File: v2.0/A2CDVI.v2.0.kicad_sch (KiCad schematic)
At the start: 33 parts, among them CON3 Apple2_edge_connector, J1 DA15_Plug, J2 Aux, U1 RPI-Pico, U2 74LVC245, U3 74LVC245, U4 74LVC245, U5 74LVC245

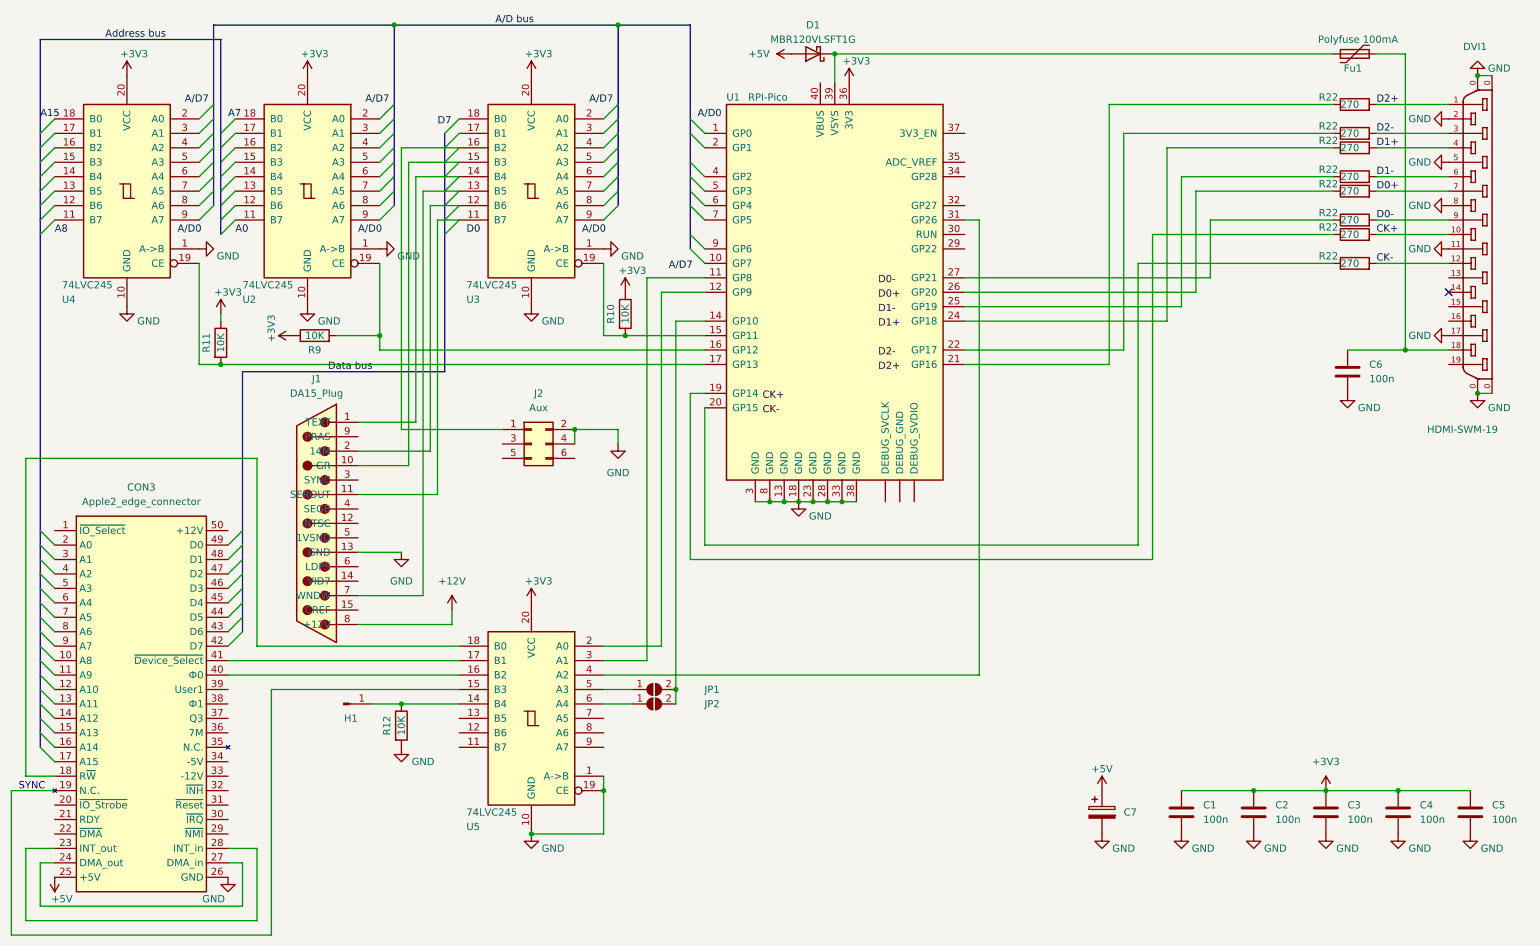
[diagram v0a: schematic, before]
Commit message: Update A2CDVI.v2.0.kicad_sch
Added components, removed Slot and extra 245 chips
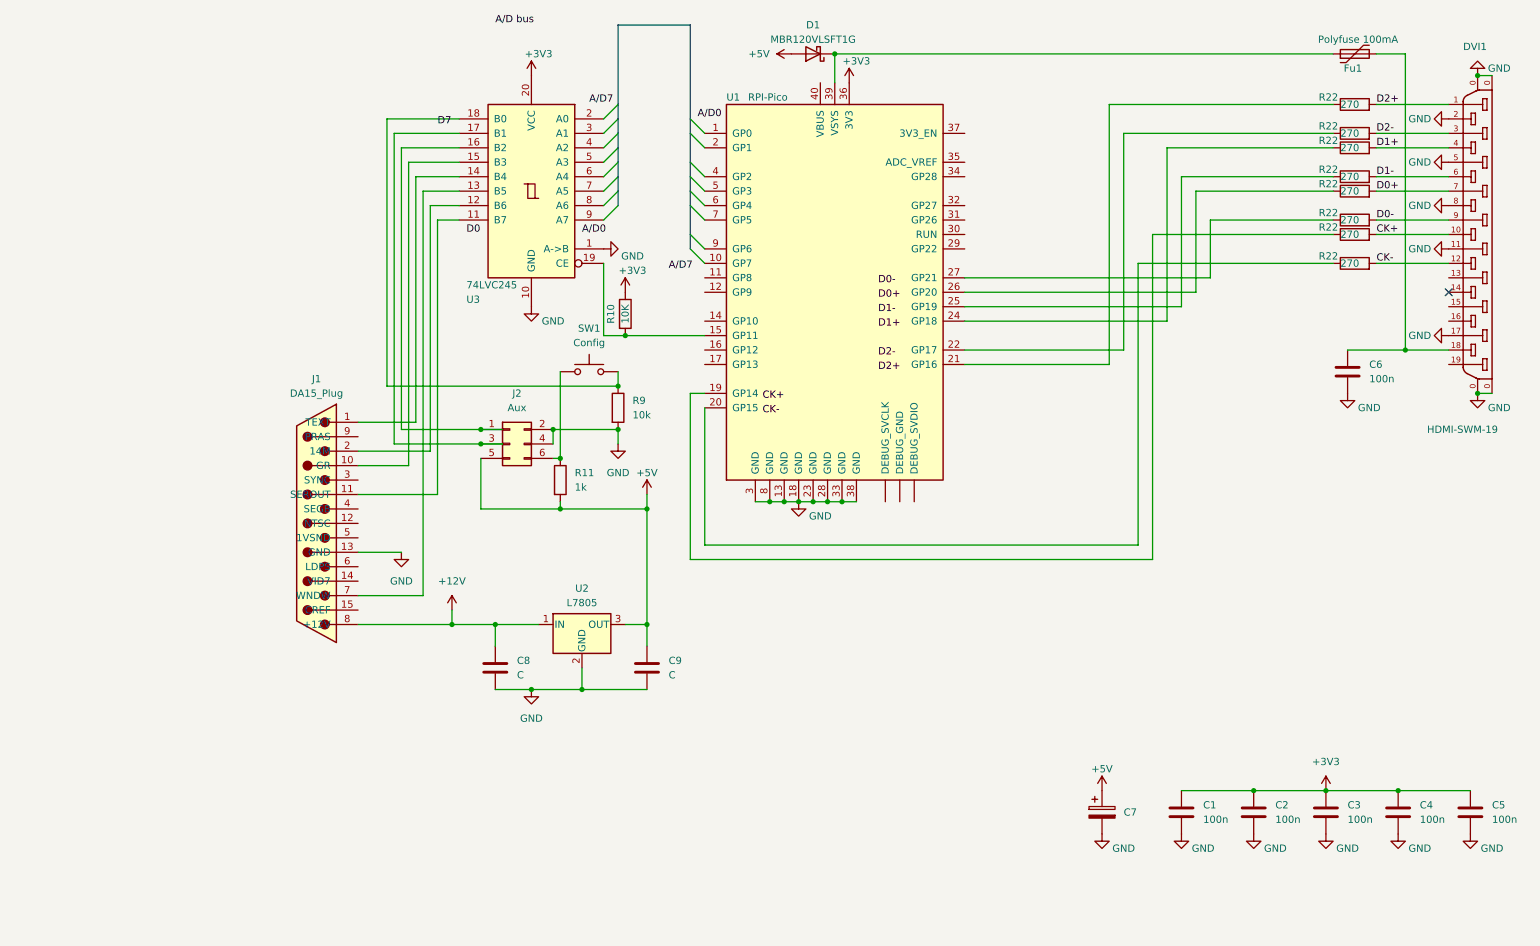
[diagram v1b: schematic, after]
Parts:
- removed CON3: Apple2_edge_connector, AppleII:Connector Apple II, symbol Ralle_Library:Apple2_edge_connector
- removed H1: Conn_01x01_Pin, symbol Connector:Conn_01x01_Pin
- removed JP1, JP2: SolderJumper_2_Open, symbol Jumper:SolderJumper_2_Open
- removed R12: 10K, Resistor_SMD:R_0402_1005Metric_Pad0.72x0.64mm_HandSolder, symbol Device:R
- removed U2, U4, U5: 74LVC245, symbol 74xx:74LS245
- added C8, C9: C, symbol Device:C
- added SW1: Config, symbol Switch:SW_Push
- added U2: L7805, symbol Regulator_Linear:L7805
- R11: value 10K -> 1k; footprint Resistor_SMD:R_0402_1005Metric_Pad0.72x0.64mm_HandSolder -> (none)
- R9: value 10K -> 10k; footprint Resistor_SMD:R_0402_1005Metric_Pad0.72x0.64mm_HandSolder -> (none)
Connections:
- net +12V: now also C8.1, U2.1 (IN)
- net +3V3: no longer R11.1, R9.1
- net +5V: now also J2.5 (Pin_5), R11.2, C9.1, U2.3 (OUT)
- net GND: now also R9.2, C8.2, C9.2, U2.2 (GND)
- net at J2.3 (Pin_3): now also U3.17 (B1)
- net at J2.6 (Pin_6): now also R11.1, SW1.1
- net at U1.17 (GP13): no longer R11.2
- net at U1.16 (GP12): no longer R9.2
- net at U3.18 (B0): now also R9.1, SW1.2
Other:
- note removed: "SYNC"
- moved on the sheet: J2

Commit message: Initial Layout mess
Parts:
- C1, C2, C3, C4, C5, C6, C8, C9: footprint (none) -> Capacitor_SMD:C_0402_1005Metric_Pad0.74x0.62mm_HandSolder
- C7: footprint (none) -> Capacitor_SMD:C_1210_3225Metric_Pad1.33x2.70mm_HandSolder
- DVI1: footprint (none) -> Connector_Video:HDMI_A_Molex_208658-1001_Horizontal
- Fu1: footprint (none) -> Fuse:Fuse_0805_2012Metric_Pad1.15x1.40mm_HandSolder
- J1: footprint (none) -> Connector_Dsub:DSUB-15_Male_Vertical_P2.77x2.84mm_MountingHoles
- J2: footprint (none) -> Connector_PinHeader_1.00mm:PinHeader_2x03_P1.00mm_Vertical
- R11, R22, R9: footprint (none) -> Resistor_SMD:R_0402_1005Metric_Pad0.72x0.64mm_HandSolder
- SW1: footprint (none) -> Button_Switch_SMD:SW_SPST_PTS645
- U1: footprint (none) -> MCU_RaspberryPi_and_Boards:RPi_Pico_SMD_TH
- U2: footprint (none) -> Package_TO_SOT_SMD:TO-252-2
- U3: footprint (none) -> Package_SO:TSSOP-20_4.4x6.5mm_P0.65mm
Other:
- moved on the sheet: C1, C2, C3, C4, C5, C7

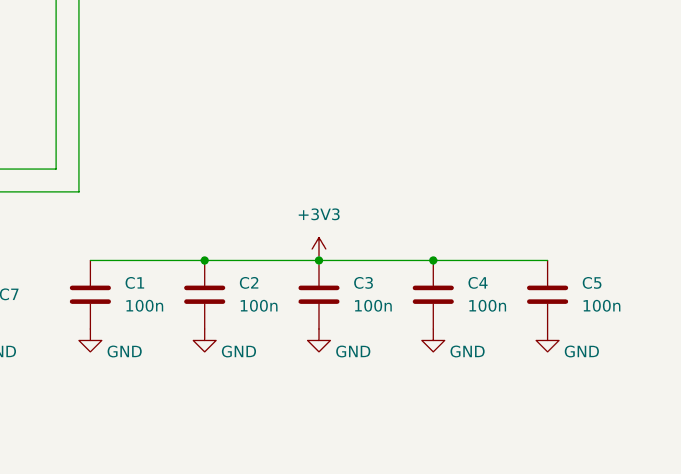
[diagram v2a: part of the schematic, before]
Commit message: Basic Board Layout
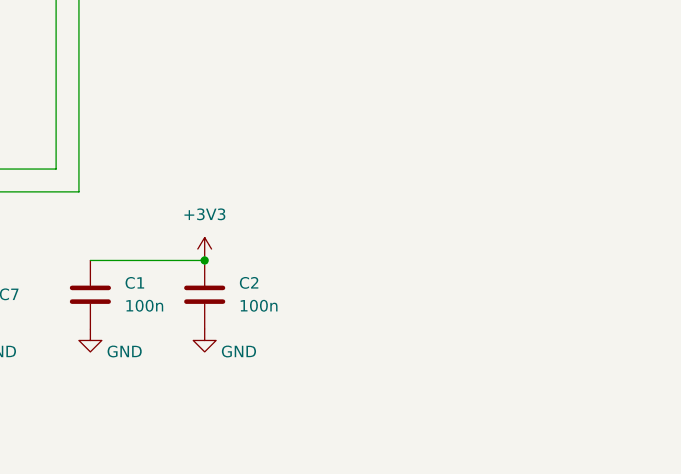
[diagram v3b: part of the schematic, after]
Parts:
- removed C3, C4, C5: 100n, Capacitor_SMD:C_0402_1005Metric_Pad0.74x0.62mm_HandSolder, symbol Device:C
- D1: footprint Diode_THT:D_DO-35_SOD27_P7.62mm_Horizontal -> Diode_SMD:D_SMA_Handsoldering
- J2: footprint Connector_PinHeader_1.00mm:PinHeader_2x03_P1.00mm_Vertical -> Connector_PinHeader_2.54mm:PinHeader_2x03_P2.54mm_Vertical
- R10, R11, R22, R9: footprint Resistor_SMD:R_0402_1005Metric_Pad0.72x0.64mm_HandSolder -> Resistor_SMD:R_0402_1005Metric
- U1: footprint MCU_RaspberryPi_and_Boards:RPi_Pico_SMD_TH -> MCU_RaspberryPi_and_Boards:RPi_Pico_SMD_TH_NO_DEBUG

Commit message: Tracks drawn
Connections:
- net +12V: now also Fu1.2; no longer J1.8 (+12V)
- net CK+: now also R22.1, U1.19 (GP14)
- net CK-: now also R22.1, U1.20 (GP15)
- net D0+: now also R22.1, U1.26 (GP20)
- net D0-: now also R22.1, U1.27 (GP21)
- net D1+: now also R22.1, U1.24 (GP18)
- net D1-: now also R22.1, U1.25 (GP19)
- net D2+: now also R22.1, U1.21 (GP16)
- net D2-: now also R22.1, U1.22 (GP17)
- net at D1.1 (K), U1.39 (VSYS): no longer Fu1.1
- net at C6.1, DVI1.18: no longer Fu1.2
- new net: Fu1.1, J1.8 (+12V)
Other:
- moved on the sheet: Fu1
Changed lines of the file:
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@@
 	)
 	(junction
-		(at 151.13 100.33)
+		(at 275.59 81.28)
 		(diameter 0)
 		(color 0 0 0 0)
 	)
 	(junction
-		(at 156.21 100.33)
+		(at 151.13 100.33)
 		(diameter 0)
 		(color 0 0 0 0)
 	)
 	(junction
-		(at 260.35 73.66)
+		(at 156.21 100.33)
 		(diameter 0)
 		(color 0 0 0 0)
@@
 		(color 0 0 0 0)
 	)
-	(junction
-		(at 160.02 21.59)
-		(diameter 0)
-		(color 0 0 0 0)
-	)
 	(no_connect
 		(at 267.97 63.5)
@@
 	(wire
 		(pts
+			(xy 88.9 121.92) (xy 92.71 121.92)
+		)
+		(stroke
+			(width 0)
+			(type default)
+		)
+	)
+	(wire
+		(pts
 			(xy 267.97 45.72) (xy 255.27 45.72)
 		)
@@
 		)
 	)
+	(wire
+		(pts
+			(xy 280.67 82.55) (xy 280.67 81.28)
+		)
+		(stroke
+			(width 0)
+			(type default)
+		)
+	)
 	(bus
 		(pts
@@
 	(wire
 		(pts
+			(xy 237.49 20.32) (xy 237.49 21.59)
+		)
+		(stroke
+			(width 0)
+			(type default)
+		)
+	)
+	(wire
+		(pts
 			(xy 100.33 133.35) (xy 106.68 133.35)
 		)
@@
 	(wire
 		(pts
-			(xy 260.35 73.66) (xy 267.97 73.66)
-		)
-		(stroke
-			(width 0)
-			(type default)
-		)
-	)
-	(wire
-		(pts
 			(xy 215.9 53.34) (xy 215.9 110.49)
 		)
@@
 	(wire
 		(pts
-			(xy 260.35 21.59) (xy 260.35 73.66)
-		)
-		(stroke
-			(width 0)
-			(type default)
-		)
-	)
-	(wire
-		(pts
 			(xy 213.36 58.42) (xy 247.65 58.42)
 		)
@@
 	(wire
 		(pts
-			(xy 123.19 71.12) (xy 137.16 71.12)
+			(xy 280.67 81.28) (xy 275.59 81.28)
 		)
 		(stroke
@@
 	(wire
 		(pts
-			(xy 255.27 21.59) (xy 260.35 21.59)
+			(xy 123.19 71.12) (xy 137.16 71.12)
 		)
 		(stroke
@@
 	(wire
 		(pts
-			(xy 160.02 21.59) (xy 247.65 21.59)
-		)
-		(stroke
-			(width 0)
-			(type default)
-		)
-	)
-	(wire
-		(pts
 			(xy 82.55 90.17) (xy 82.55 35.56)
 		)
@@
 	(wire
 		(pts
-			(xy 250.19 73.66) (xy 260.35 73.66)
+			(xy 250.19 73.66) (xy 267.97 73.66)
 		)
 		(stroke
@@
 	(wire
 		(pts
-			(xy 76.2 121.92) (xy 92.71 121.92)
+			(xy 273.05 82.55) (xy 273.05 81.28)
+		)
+		(stroke
+			(width 0)
+			(type default)
+		)
+	)
+	(wire
+		(pts
+			(xy 76.2 121.92) (xy 81.28 121.92)
 		)
 		(stroke
@@
 	)
 	(label "CK-"
-		(at 147.32 85.09 0)
+		(at 137.16 86.36 0)
+		(fields_autoplaced yes)
+		(effects
+			(font
+				(size 1.27 1.27)
+			)
+			(justify left bottom)
+		)
+	)
+	(label "D2+"
+		(at 182.88 76.2 0)
 		(fields_autoplaced yes)
 		(effects
@@
 	)
 	(label "D1-"
-		(at 167.64 67.31 0)
+		(at 182.88 66.04 0)
 		(fields_autoplaced yes)
 		(effects
@@
 	)
 	(label "D0-"
-		(at 167.64 62.23 0)
+		(at 182.88 60.96 0)
 		(fields_autoplaced yes)
 		(effects
@@
 	)
 	(label "D0+"
-		(at 167.64 64.77 0)
+		(at 182.88 63.5 0)
 		(fields_autoplaced yes)
 		(effects
@@
 	)
 	(label "CK+"
-		(at 147.32 82.55 0)
+		(at 134.62 81.28 0)
+		(fields_autoplaced yes)
+		(effects
+			(font
+				(size 1.27 1.27)
+			)
+			(justify left bottom)
+		)
+	)
+	(label "D2-"
+		(at 182.88 73.66 0)
 		(fields_autoplaced yes)
 		(effects
@@
 	)
 	(label "D1+"
-		(at 167.64 69.85 0)
+		(at 182.88 68.58 0)
 		(fields_autoplaced yes)
 		(effects
@@
 	(symbol
 		(lib_id "Neo6502_Rev_B:GND")
+		(at 280.67 82.55 0)
+		(unit 1)
+		(exclude_from_sim no)
+		(in_bom yes)
+		(on_board yes)
+		(dnp no)
+		(property "Reference" "#PWR08"
+			(at 280.67 88.9 0)
+			(effects
+				(font
+					(size 1.27 1.27)
+				)
+				(hide yes)
+			)
+		)
+		(property "Value" "GND"
+			(at 280.67 87.63 90)
+			(effects
+				(font
+					(size 1.27 1.27)
+				)
+			)
+		)
+		(property "Footprint" ""
+			(at 280.67 82.55 0)
+			(effects
+				(font
+					(size 1.524 1.524)
+				)
+			)
+		)
+		(property "Datasheet" ""
+			(at 280.67 82.55 0)
+			(effects
+				(font
+					(size 1.524 1.524)
+				)
+			)
+		)
+		(property "Description" ""
+			(at 280.67 82.55 0)
+			(effects
+				(font
+					(size 1.27 1.27)
+				)
+				(hide yes)
+			)
+		)
+		(pin "1"
+		)
+		(instances
+			(project "A2CDVI.v2.0"
+				(path "/4c6c2bca-2dd1-4d7b-a3c3-50b1d850646e"
+					(reference "#PWR08")
+					(unit 1)
+				)
+			)
+		)
+	)
+	(symbol
+		(lib_id "Neo6502_Rev_B:GND")
 		(at 267.97 40.64 270)
 		(mirror x)
@@
 	(symbol
 		(lib_id "Device:Polyfuse")
-		(at 251.46 21.59 90)
+		(at 85.09 121.92 90)
 		(unit 1)
 		(exclude_from_sim no)
@@
 		(dnp no)
 		(property "Reference" "Fu1"
-			(at 252.73 24.13 90)
+			(at 86.36 124.46 90)
 			(effects
 				(font
@@
 		)
 		(property "Value" "Polyfuse 100mA"
-			(at 259.08 19.05 90)
+			(at 92.71 119.38 90)
 			(effects
 				(font
@@
 		)
 		(property "Footprint" "Fuse:Fuse_0805_2012Metric_Pad1.15x1.40mm_HandSolder"
-			(at 256.54 20.32 0)
+			(at 90.17 120.65 0)
 			(effects
 				(font
@@
 		)
 		(property "Datasheet" "MF-R020"
-			(at 251.46 21.59 0)
+			(at 85.09 121.92 0)
 			(effects
 				(font
@@
 		)
 		(property "Description" ""
-			(at 251.46 21.59 0)
+			(at 85.09 121.92 0)
 			(effects
 				(font
@@
 	(symbol
 		(lib_id "Neo6502_Rev_B:GND")
-		(at 273.05 81.28 0)
+		(at 273.05 82.55 0)
 		(mirror y)
 		(unit 1)
@@
 		(dnp no)
 		(property "Reference" "#PWR?"
-			(at 273.05 87.63 0)
+			(at 273.05 88.9 0)
 			(effects
 				(font
@@
 		)
 		(property "Value" "GND"
-			(at 276.86 83.82 0)
+			(at 276.86 85.09 0)
 			(effects
 				(font
@@
 		)
 		(property "Footprint" ""
-			(at 273.05 81.28 0)
+			(at 273.05 82.55 0)
 			(effects
 				(font
@@
 		)
 		(property "Datasheet" ""
-			(at 273.05 81.28 0)
+			(at 273.05 82.55 0)
 			(effects
 				(font
@@
 		)
 		(property "Description" ""
-			(at 273.05 81.28 0)
+			(at 273.05 82.55 0)
 			(effects
 				(font

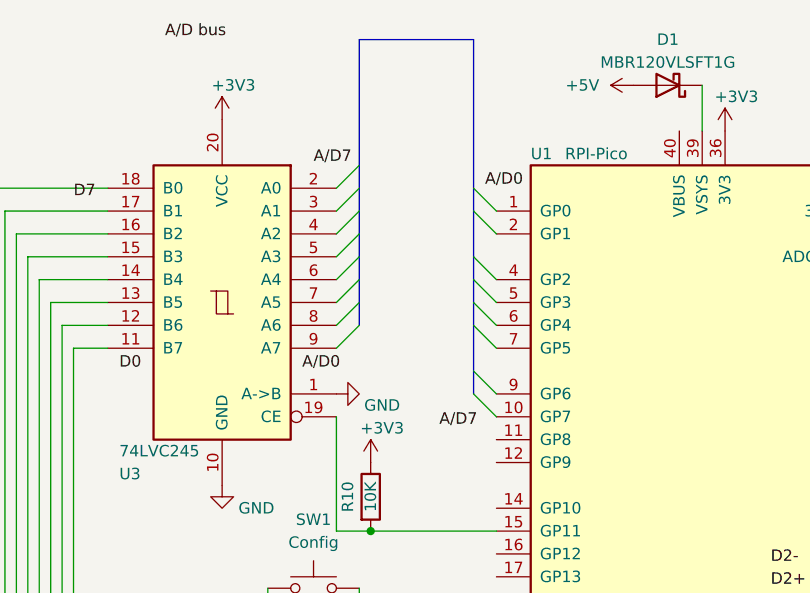
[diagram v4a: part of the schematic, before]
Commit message: Fixed missing connections in schematic
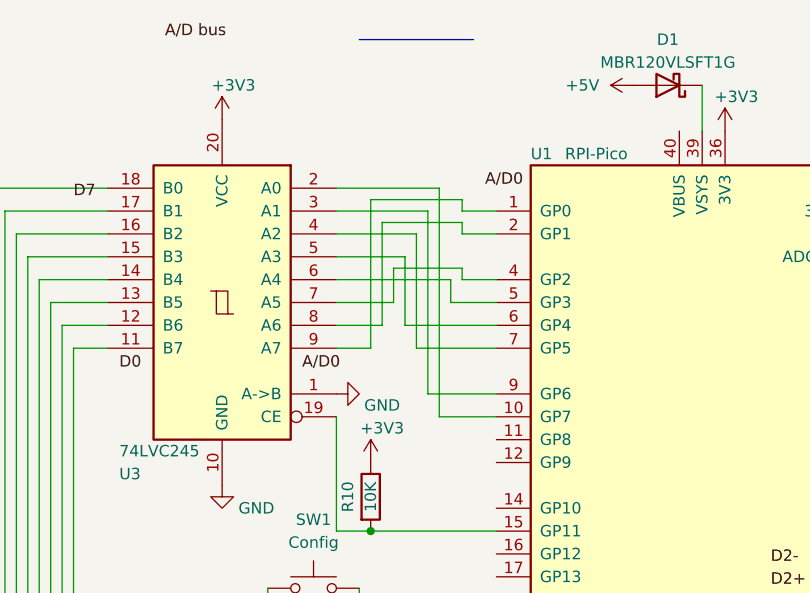
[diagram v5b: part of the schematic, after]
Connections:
- net at U1.1 (GP0): now also U3.9 (A7)
- net at U1.10 (GP7): now also U3.2 (A0)
- net at U1.2 (GP1): now also U3.8 (A6)
- net at U1.4 (GP2): now also U3.7 (A5)
- net at U1.5 (GP3): now also U3.6 (A4)
- net at U1.6 (GP4): now also U3.5 (A3)
- net at U1.7 (GP5): now also U3.4 (A2)
- net at U1.9 (GP6): now also U3.3 (A1)
